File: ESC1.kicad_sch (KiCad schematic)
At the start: 34 parts, among them J7 SWD1, J8 MOTOR1, Q2 XRS306D, Q3 XRS306D, Q4 XRS306D, U7 STM32G071GBUxN, U8 DRV8300D

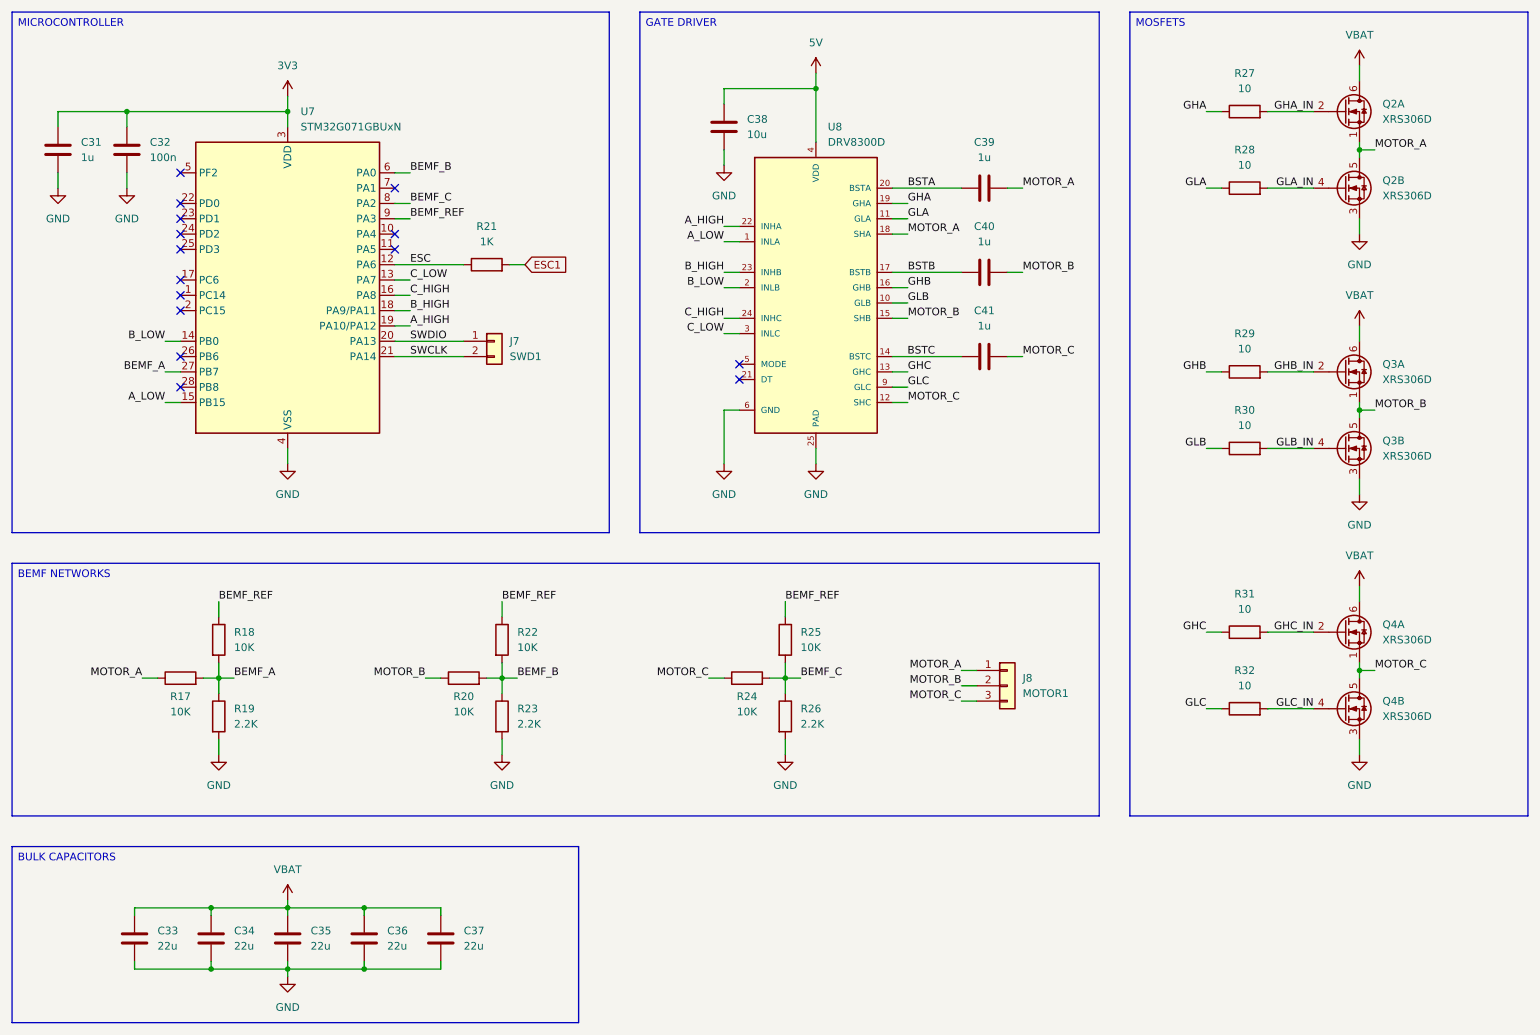
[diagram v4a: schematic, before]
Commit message: Voltage detection
Added a VBUS voltage detection for the RP.
Minor layout changes.
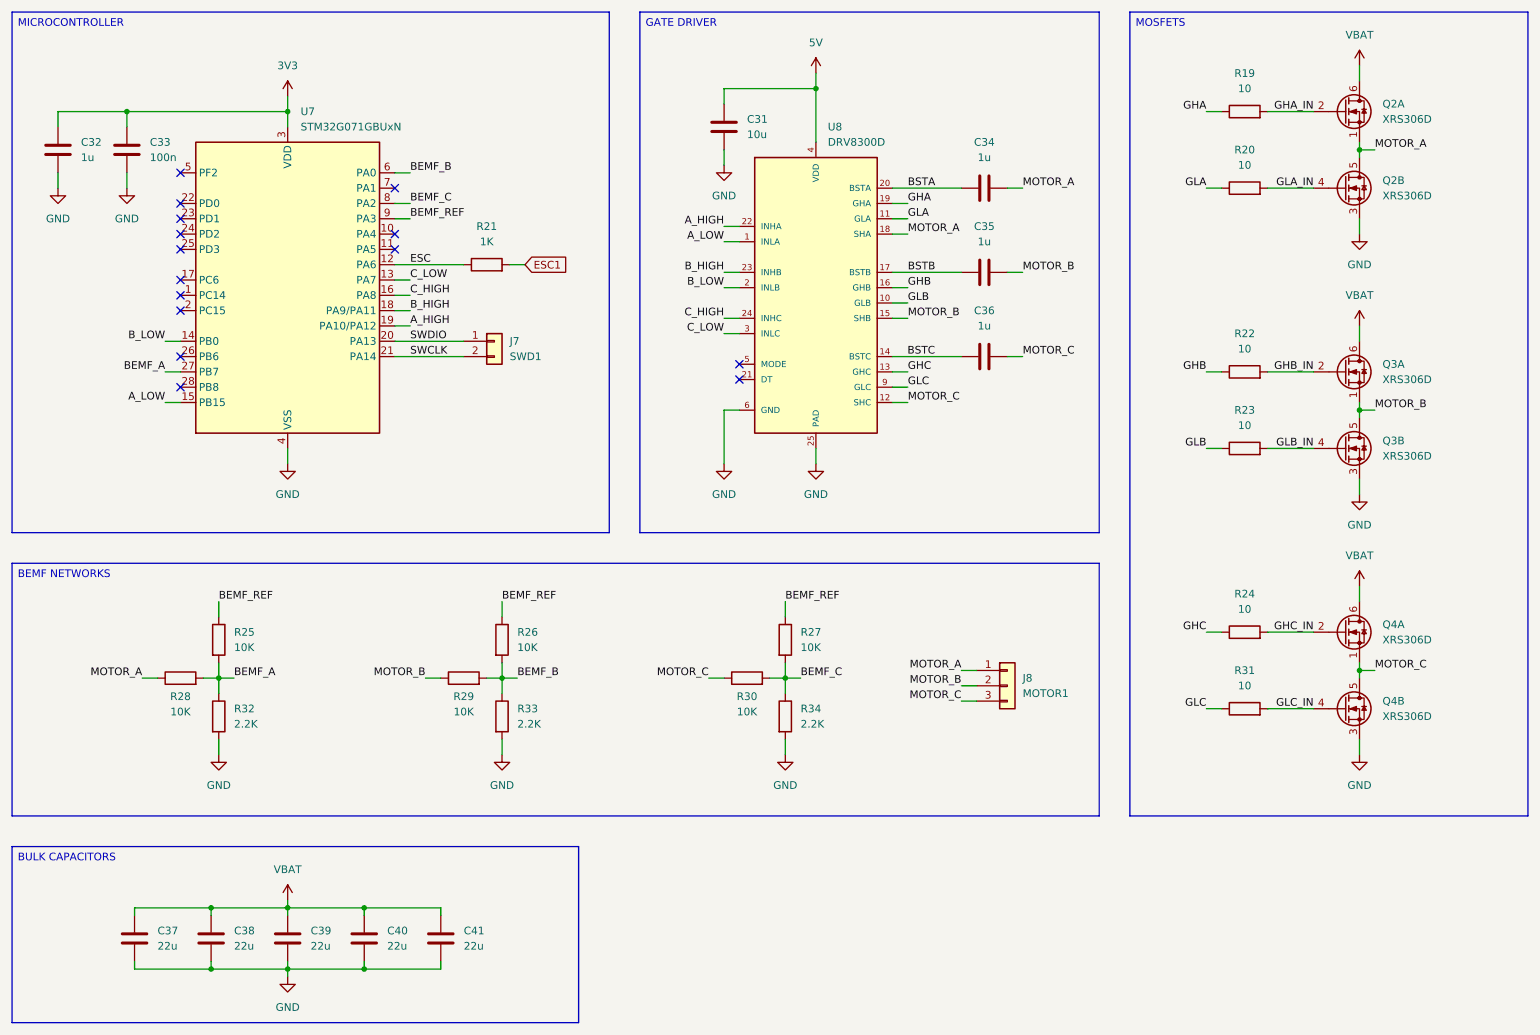
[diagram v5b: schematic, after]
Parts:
- renumbered C38 to C31, C31 to C32, C32 to C33, C39 to C34, C40 to C35, C41 to C36, C33 to C37, C34 to C38, C35 to C39, C36 to C40, C37 to C41, R27 to R19, R28 to R20, R29 to R22, R30 to R23, R31 to R24, R18 to R25, R22 to R26, R25 to R27, R17 to R28, R20 to R29, R24 to R30, R32 to R31, R19 to R32, R23 to R33, R26 to R34
